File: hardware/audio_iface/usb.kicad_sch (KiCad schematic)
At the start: 2 parts, among them J401 USB_C_Receptacle_USB2.0, U401 USBLC6-2SC6

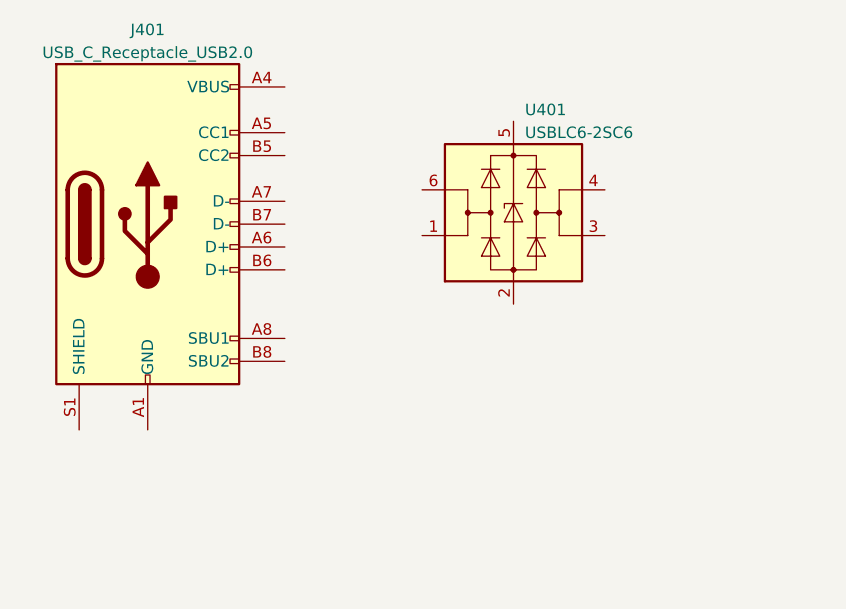
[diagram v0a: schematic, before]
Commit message: added some connections
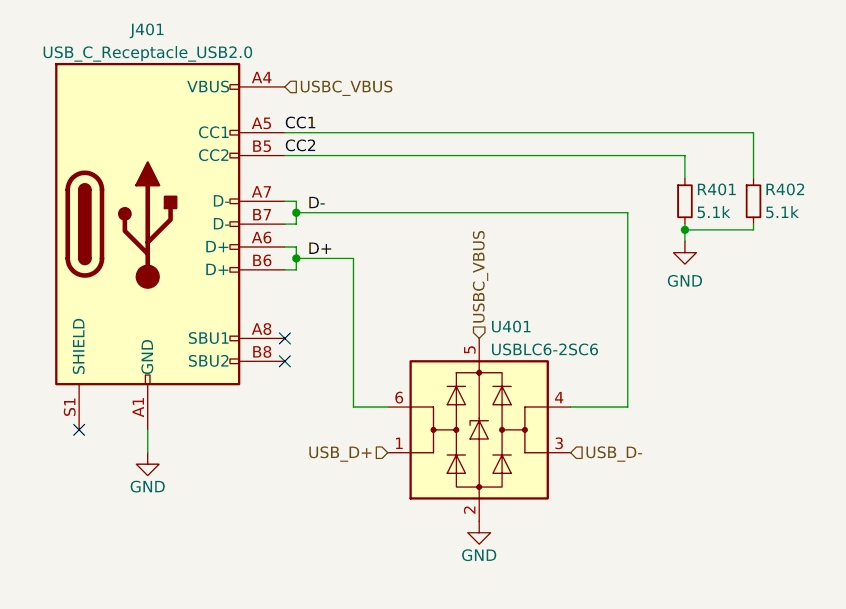
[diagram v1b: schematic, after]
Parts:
- added R401, R402: 5.1k, Resistor_SMD:R_0402_1005Metric, symbol Device:R_Small
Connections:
- net GND: now reaches J401.A1 (GND), J401.A12 (GND), J401.B1 (GND), J401.B12 (GND)
- net GND: now also U401.2 (GND), R401.2, R402.2
- net USBC_VBUS: now reaches J401.A4 (VBUS), J401.A9 (VBUS), J401.B4 (VBUS), J401.B9 (VBUS)
- net USBC_VBUS: now also U401.5 (VBUS)
- net CC1: now reaches J401.A5 (CC1)
- net CC1: now also R402.1
- net D+: now reaches J401.A6 (D+)
- net D+: now also J401.B6 (D+), U401.6 (I/O1)
- net D-: now reaches J401.A7 (D-)
- net D-: now also J401.B7 (D-), U401.4 (I/O2)
- net CC2: now reaches J401.B5 (CC2)
- net CC2: now also R401.1
- net USB_D+: now reaches U401.1 (I/O1)
- net USB_D-: now reaches U401.3 (I/O2)
- no-connect marks 0 -> 3
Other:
- moved on the sheet: U401

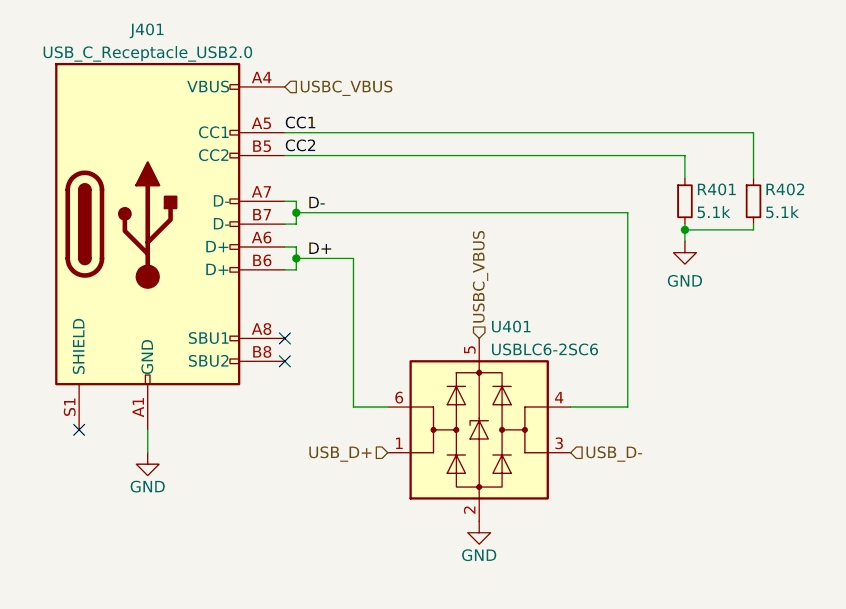
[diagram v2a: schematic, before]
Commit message: add logo
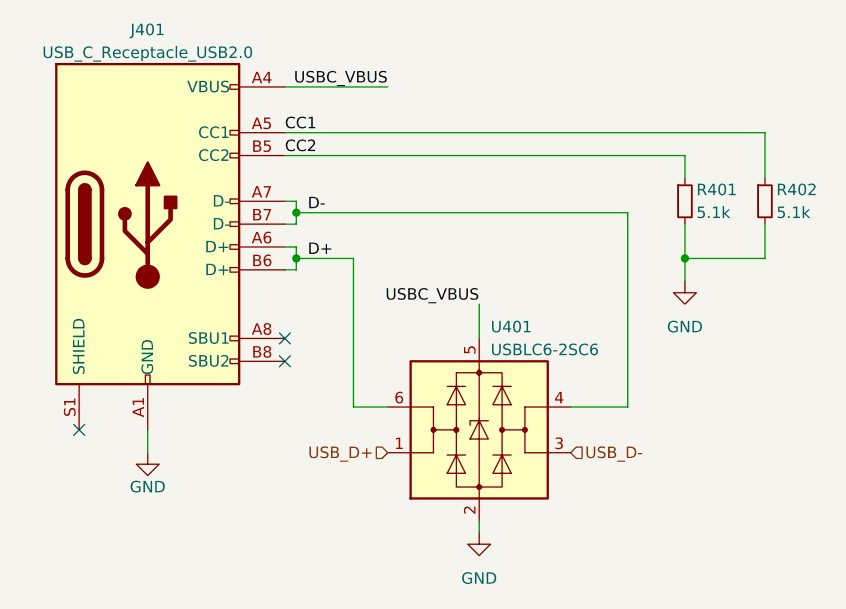
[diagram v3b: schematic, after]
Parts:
- R401, R402: LCSC Part (none) -> C2906948
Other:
- moved on the sheet: R402
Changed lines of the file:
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@@
   (junction (at 124.46 77.47) (diameter 0) (color 0 0 0 0)
   )
+  (junction (at 167.64 82.55) (diameter 0) (color 0 0 0 0)
+  )
   (junction (at 124.46 82.55) (diameter 0) (color 0 0 0 0)
-  )
-  (junction (at 167.64 79.375) (diameter 0) (color 0 0 0 0)
   )
   (no_connect (at 100.33 101.6))
   (no_connect (at 123.19 91.44))
   (no_connect (at 123.19 93.98))
+  (wire (pts (xy 134.62 63.5) (xy 123.19 63.5))
+    (stroke (width 0) (type default))
+  )
   (wire (pts (xy 161.29 77.47) (xy 161.29 99.06))
     (stroke (width 0) (type default))
   )
-  (wire (pts (xy 175.26 79.375) (xy 175.26 78.74))
+  (wire (pts (xy 176.53 82.55) (xy 176.53 78.74))
     (stroke (width 0) (type default))
   )
@@
     (stroke (width 0) (type default))
   )
-  (wire (pts (xy 123.19 68.58) (xy 175.26 68.58))
+  (wire (pts (xy 123.19 68.58) (xy 176.53 68.58))
     (stroke (width 0) (type default))
   )
@@
     (stroke (width 0) (type default))
   )
-  (wire (pts (xy 175.26 68.58) (xy 175.26 73.66))
-    (stroke (width 0) (type default))
-  )
-  (wire (pts (xy 167.64 78.74) (xy 167.64 79.375))
+  (wire (pts (xy 176.53 68.58) (xy 176.53 73.66))
+    (stroke (width 0) (type default))
+  )
+  (wire (pts (xy 144.78 87.63) (xy 144.78 91.44))
     (stroke (width 0) (type default))
   )
@@
     (stroke (width 0) (type default))
   )
-  (wire (pts (xy 167.64 79.375) (xy 175.26 79.375))
+  (wire (pts (xy 167.64 82.55) (xy 167.64 85.09))
+    (stroke (width 0) (type default))
+  )
+  (wire (pts (xy 144.78 111.76) (xy 144.78 113.03))
+    (stroke (width 0) (type default))
+  )
+  (wire (pts (xy 167.64 82.55) (xy 176.53 82.55))
     (stroke (width 0) (type default))
   )
@@
     (stroke (width 0) (type default))
   )
-  (wire (pts (xy 167.64 79.375) (xy 167.64 80.645))
+  (wire (pts (xy 167.64 78.74) (xy 167.64 82.55))
     (stroke (width 0) (type default))
   )
@@
     (effects (font (size 1.27 1.27)) (justify left bottom))
   )
+  (label "USBC_VBUS" (at 144.78 87.63 180) (fields_autoplaced)
+    (effects (font (size 1.27 1.27)) (justify right bottom))
+  )
   (label "CC2" (at 123.19 71.12 0) (fields_autoplaced)
     (effects (font (size 1.27 1.27)) (justify left bottom))
@@
     (effects (font (size 1.27 1.27)) (justify left bottom))
   )
+  (label "USBC_VBUS" (at 134.62 63.5 180) (fields_autoplaced)
+    (effects (font (size 1.27 1.27)) (justify right bottom))
+  )
   (label "D+" (at 125.73 82.55 0) (fields_autoplaced)
     (effects (font (size 1.27 1.27)) (justify left bottom))
-  )
-  (hierarchical_label "USBC_VBUS" (shape input) (at 144.78 91.44 90) (fields_autoplaced)
-    (effects (font (size 1.27 1.27)) (justify left))
   )
   (hierarchical_label "USB_D+" (shape input) (at 134.62 104.14 180) (fields_autoplaced)
     (effects (font (size 1.27 1.27)) (justify right))
   )
-  (hierarchical_label "USBC_VBUS" (shape input) (at 123.19 63.5 0) (fields_autoplaced)
-    (effects (font (size 1.27 1.27)) (justify left))
-  )
   (hierarchical_label "USB_D-" (shape input) (at 154.94 104.14 0) (fields_autoplaced)
     (effects (font (size 1.27 1.27)) (justify left))
   )
-  (symbol (lib_id "Device:R_Small") (at 175.26 76.2 0) (unit 1)
+  (symbol (lib_id "Device:R_Small") (at 176.53 76.2 0) (unit 1)
     (in_bom yes) (on_board yes) (dnp no)
-    (property "Reference" "R402" (at 176.53 74.93 0)
-      (effects (font (size 1.27 1.27)) (justify left))
-    )
-    (property "Value" "5.1k" (at 176.53 77.47 0)
-      (effects (font (size 1.27 1.27)) (justify left))
-    )
-    (property "Footprint" "Resistor_SMD:R_0402_1005Metric" (at 175.26 76.2 0)
-      (effects (font (size 1.27 1.27)) hide)
-    )
-    (property "Datasheet" "~" (at 175.26 76.2 0)
+    (property "Reference" "R402" (at 177.8 74.93 0)
+      (effects (font (size 1.27 1.27)) (justify left))
+    )
+    (property "Value" "5.1k" (at 177.8 77.47 0)
+      (effects (font (size 1.27 1.27)) (justify left))
+    )
+    (property "Footprint" "Resistor_SMD:R_0402_1005Metric" (at 176.53 76.2 0)
+      (effects (font (size 1.27 1.27)) hide)
+    )
+    (property "Datasheet" "~" (at 176.53 76.2 0)
+      (effects (font (size 1.27 1.27)) hide)
+    )
+    (property "LCSC Part" "C2906948" (at 176.53 76.2 0)
       (effects (font (size 1.27 1.27)) hide)
     )
@@
     )
   )
-  (symbol (lib_id "power:GND") (at 144.78 111.76 0) (unit 1)
-    (in_bom yes) (on_board yes) (dnp no)
-    (property "Reference" "#PWR0402" (at 144.78 118.11 0)
-      (effects (font (size 1.27 1.27)) hide)
-    )
-    (property "Value" "GND" (at 144.78 115.57 0)
-      (effects (font (size 1.27 1.27)))
-    )
-    (property "Footprint" "" (at 144.78 111.76 0)
-      (effects (font (size 1.27 1.27)) hide)
-    )
-    (property "Datasheet" "" (at 144.78 111.76 0)
+  (symbol (lib_name "GND_2") (lib_id "power:GND") (at 144.78 113.03 0) (unit 1)
+    (in_bom yes) (on_board yes) (dnp no) (fields_autoplaced)
+    (property "Reference" "#PWR0402" (at 144.78 119.38 0)
+      (effects (font (size 1.27 1.27)) hide)
+    )
+    (property "Value" "GND" (at 144.78 118.11 0)
+      (effects (font (size 1.27 1.27)))
+    )
+    (property "Footprint" "" (at 144.78 113.03 0)
+      (effects (font (size 1.27 1.27)) hide)
+    )
+    (property "Datasheet" "" (at 144.78 113.03 0)
       (effects (font (size 1.27 1.27)) hide)
     )
@@
         )
       )
-      (project "test_SGTL5000"
-        (path "/ac48c67b-93af-4f94-918a-70ca90985cf2/9cab4440-8408-40f0-b978-06230ea8030a"
-          (reference "#PWR0402") (unit 1)
+    )
+  )
+  (symbol (lib_name "GND_2") (lib_id "power:GND") (at 167.64 85.09 0) (unit 1)
+    (in_bom yes) (on_board yes) (dnp no) (fields_autoplaced)
+    (property "Reference" "#PWR0403" (at 167.64 91.44 0)
+      (effects (font (size 1.27 1.27)) hide)
+    )
+    (property "Value" "GND" (at 167.64 90.17 0)
+      (effects (font (size 1.27 1.27)))
+    )
+    (property "Footprint" "" (at 167.64 85.09 0)
+      (effects (font (size 1.27 1.27)) hide)
+    )
+    (property "Datasheet" "" (at 167.64 85.09 0)
+      (effects (font (size 1.27 1.27)) hide)
+    )
+    (pin "1")
+    (instances
+      (project "audio_iface"
+        (path "/84adbf2e-65c7-4710-86f9-725cae0256c9/f8f73879-1c97-4949-a7e6-1a88ad2aef24"
+          (reference "#PWR0403") (unit 1)
         )
       )
@@
     )
   )
-  (symbol (lib_id "power:GND") (at 167.64 80.645 0) (unit 1)
-    (in_bom yes) (on_board yes) (dnp no)
-    (property "Reference" "#PWR0403" (at 167.64 86.995 0)
-      (effects (font (size 1.27 1.27)) hide)
-    )
-    (property "Value" "GND" (at 167.64 85.09 0)
-      (effects (font (size 1.27 1.27)))
-    )
-    (property "Footprint" "" (at 167.64 80.645 0)
-      (effects (font (size 1.27 1.27)) hide)
-    )
-    (property "Datasheet" "" (at 167.64 80.645 0)
-      (effects (font (size 1.27 1.27)) hide)
-    )
-    (pin "1")
-    (instances
-      (project "audio_iface"
-        (path "/84adbf2e-65c7-4710-86f9-725cae0256c9/f8f73879-1c97-4949-a7e6-1a88ad2aef24"
-          (reference "#PWR0403") (unit 1)
-        )
-      )
-      (project "test_SGTL5000"
-        (path "/ac48c67b-93af-4f94-918a-70ca90985cf2/9cab4440-8408-40f0-b978-06230ea8030a"
-          (reference "#PWR0403") (unit 1)
-        )
-      )
-    )
-  )
   (symbol (lib_id "Device:R_Small") (at 167.64 76.2 0) (unit 1)
     (in_bom yes) (on_board yes) (dnp no)
@@
       (effects (font (size 1.27 1.27)) hide)
     )
+    (property "LCSC Part" "C2906948" (at 167.64 76.2 0)
+      (effects (font (size 1.27 1.27)) hide)
+    )
